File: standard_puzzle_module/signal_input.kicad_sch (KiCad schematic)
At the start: 6 parts, among them J9 Screw_Terminal_01x04

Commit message: chore: clean up
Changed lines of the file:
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@@
+	)
+	(junction
+		(at 134.62 107.95)
+		(diameter 0)
+		(color 0 0 0 0)
+	)
+	(junction
+		(at 134.62 96.52)
+		(diameter 0)
+		(color 0 0 0 0)
 	)
 	(junction
@@
 		(color 0 0 0 0)
 	)
-	(junction
-		(at 134.62 107.95)
-		(diameter 0)
-		(color 0 0 0 0)
-	)
-	(junction
-		(at 134.62 96.52)
-		(diameter 0)
-		(color 0 0 0 0)
-	)
 	(wire
 		(pts
@@
 	(wire
 		(pts
-			(xy 119.38 104.14) (xy 119.38 107.95)
+			(xy 102.87 107.95) (xy 119.38 107.95)
+		)
+		(stroke
+			(width 0)
+			(type default)
+		)
+	)
+	(wire
+		(pts
+			(xy 119.38 96.52) (xy 119.38 107.95)
 		)
 		(stroke
@@
 		(pts
 			(xy 147.32 107.95) (xy 162.56 107.95)
+		)
+		(stroke
+			(width 0)
+			(type default)
+		)
+	)
+	(wire
+		(pts
+			(xy 102.87 96.52) (xy 102.87 107.95)
 		)
 		(stroke
@@
 	(global_label "GPIO"
 		(shape input)
-		(at 119.38 104.14 90)
+		(at 119.38 96.52 90)
 		(fields_autoplaced yes)
 		(effects
@@
 		)
 		(property "Intersheetrefs" "${INTERSHEET_REFS}"
-			(at 119.38 96.6795 90)
+			(at 119.38 89.0595 90)
 			(hide yes)
 			(show_name no)
@@
 		)
 	)
+	(hierarchical_label "signal_input"
+		(shape output)
+		(at 102.87 96.52 0)
+		(effects
+			(font
+				(size 1.27 1.27)
+			)
+			(justify left)
+		)
+	)

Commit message: feat: clean up schematic references and run clean annotation
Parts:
- CC_SIN1: renamed from C13; footprint (none) -> Capacitor_THT:C_Disc_D5.0mm_W2.5mm_P5.00mm
- J_SIN1: renamed from J9; value Screw_Terminal_01x04 -> SIGNAL IN; footprint (none) -> TerminalBlock_Phoenix:TerminalBlock_Phoenix_MKDS-1,5-4-5.08_1x04_P5.08mm_Horizontal
- R_SIN1: renamed from R18; value 100 kOhm -> 100kOhm; footprint (none) -> Resistor_THT:R_Axial_DIN0411_L9.9mm_D3.6mm_P15.24mm_Horizontal
- R_SIN2: renamed from R19; value 4.7 kOhm -> 4.7kOhm; footprint (none) -> Resistor_THT:R_Axial_DIN0411_L9.9mm_D3.6mm_P15.24mm_Horizontal
- renumbered D9 to D_SCHSIN1, D10 to D_SCHSIN2
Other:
- moved on the sheet: CC_SIN1
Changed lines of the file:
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@@
 	(wire
 		(pts
-			(xy 119.38 120.65) (xy 119.38 118.11)
+			(xy 119.38 120.65) (xy 119.38 119.38)
 		)
 		(stroke
@@
 	(wire
 		(pts
-			(xy 119.38 110.49) (xy 119.38 107.95)
+			(xy 119.38 111.76) (xy 119.38 107.95)
 		)
 		(stroke
@@
 		(dnp no)
 		(fields_autoplaced yes)
-		(property "Reference" "J9"
+		(property "Reference" "J_SIN1"
 			(at 170.18 105.4099 0)
 			(show_name no)
@@
 			)
 		)
-		(property "Value" "Screw_Terminal_01x04"
+		(property "Value" "SIGNAL IN"
 			(at 170.18 107.9499 0)
 			(show_name no)
@@
 			)
 		)
-		(property "Footprint" ""
+		(property "Footprint" "TerminalBlock_Phoenix:TerminalBlock_Phoenix_MKDS-1,5-4-5.08_1x04_P5.08mm_Horizontal"
 			(at 167.64 105.41 0)
 			(hide yes)
@@
 		(instances
 			(project "standard_puzzle_box"
-				(path "/13314f97-080e-4924-a8fe-b4d224920625/c0b0d7d0-33da-4714-9ac3-d3e577314e9e"
-					(reference "J11")
+				(path "/13314f97-080e-4924-a8fe-b4d224920625/b204176e-3230-48f0-bf70-6ca27eccae57"
+					(reference "J_SIN2")
 					(unit 1)
 				)
 				(path "/13314f97-080e-4924-a8fe-b4d224920625/c2e63cb3-71db-41cb-b6d8-62c7e6a89138"
-					(reference "J9")
+					(reference "J_SIN1")
 					(unit 1)
 				)
@@
 		(dnp no)
 		(fields_autoplaced yes)
-		(property "Reference" "R19"
+		(property "Reference" "R_SIN2"
 			(at 143.51 101.6 90)
 			(show_name no)
@@
 			)
 		)
-		(property "Value" "4.7 kOhm"
+		(property "Value" "4.7kOhm"
 			(at 143.51 104.14 90)
 			(show_name no)
@@
 			)
 		)
-		(property "Footprint" ""
+		(property "Footprint" "Resistor_THT:R_Axial_DIN0411_L9.9mm_D3.6mm_P15.24mm_Horizontal"
 			(at 143.51 106.172 90)
 			(hide yes)
@@
 		(instances
 			(project "standard_puzzle_box"
-				(path "/13314f97-080e-4924-a8fe-b4d224920625/c0b0d7d0-33da-4714-9ac3-d3e577314e9e"
-					(reference "R21")
+				(path "/13314f97-080e-4924-a8fe-b4d224920625/b204176e-3230-48f0-bf70-6ca27eccae57"
+					(reference "R_SIN4")
 					(unit 1)
 				)
 				(path "/13314f97-080e-4924-a8fe-b4d224920625/c2e63cb3-71db-41cb-b6d8-62c7e6a89138"
-					(reference "R19")
+					(reference "R_SIN2")
 					(unit 1)
 				)
@@
 		(instances
 			(project "standard_puzzle_box"
-				(path "/13314f97-080e-4924-a8fe-b4d224920625/c0b0d7d0-33da-4714-9ac3-d3e577314e9e"
-					(reference "#PWR051")
+				(path "/13314f97-080e-4924-a8fe-b4d224920625/b204176e-3230-48f0-bf70-6ca27eccae57"
+					(reference "#PWR01")
 					(unit 1)
 				)
@@
 		)
 		(property "Value" "+3.3V"
-			(at 144.526 90.17 0)
+			(at 148.59 95.25 0)
 			(show_name no)
 			(do_not_autoplace no)
@@
 		(instances
 			(project "standard_puzzle_box"
-				(path "/13314f97-080e-4924-a8fe-b4d224920625/c0b0d7d0-33da-4714-9ac3-d3e577314e9e"
-					(reference "#PWR054")
+				(path "/13314f97-080e-4924-a8fe-b4d224920625/b204176e-3230-48f0-bf70-6ca27eccae57"
+					(reference "#PWR011")
 					(unit 1)
 				)
@@
 		(instances
 			(project "standard_puzzle_box"
-				(path "/13314f97-080e-4924-a8fe-b4d224920625/c0b0d7d0-33da-4714-9ac3-d3e577314e9e"
-					(reference "#PWR052")
+				(path "/13314f97-080e-4924-a8fe-b4d224920625/b204176e-3230-48f0-bf70-6ca27eccae57"
+					(reference "#PWR09")
 					(unit 1)
 				)
@@
 		(in_pos_files yes)
 		(dnp no)
-		(fields_autoplaced yes)
-		(property "Reference" "D10"
-			(at 140.0175 90.17 0)
+		(property "Reference" "D_SCHSIN2"
+			(at 140.97 90.17 0)
 			(show_name no)
 			(do_not_autoplace no)
@@
 		(instances
 			(project "standard_puzzle_box"
-				(path "/13314f97-080e-4924-a8fe-b4d224920625/c0b0d7d0-33da-4714-9ac3-d3e577314e9e"
-					(reference "D14")
+				(path "/13314f97-080e-4924-a8fe-b4d224920625/b204176e-3230-48f0-bf70-6ca27eccae57"
+					(reference "D_SCHSIN4")
 					(unit 1)
 				)
 				(path "/13314f97-080e-4924-a8fe-b4d224920625/c2e63cb3-71db-41cb-b6d8-62c7e6a89138"
-					(reference "D10")
+					(reference "D_SCHSIN2")
 					(unit 1)
 				)
@@
 		(in_pos_files yes)
 		(dnp no)
-		(fields_autoplaced yes)
-		(property "Reference" "D9"
-			(at 129.8575 90.17 0)
+		(property "Reference" "D_SCHSIN1"
+			(at 128.27 90.17 0)
 			(show_name no)
 			(do_not_autoplace no)
@@
 		(instances
 			(project "standard_puzzle_box"
-				(path "/13314f97-080e-4924-a8fe-b4d224920625/c0b0d7d0-33da-4714-9ac3-d3e577314e9e"
-					(reference "D13")
+				(path "/13314f97-080e-4924-a8fe-b4d224920625/b204176e-3230-48f0-bf70-6ca27eccae57"
+					(reference "D_SCHSIN3")
 					(unit 1)
 				)
 				(path "/13314f97-080e-4924-a8fe-b4d224920625/c2e63cb3-71db-41cb-b6d8-62c7e6a89138"
-					(reference "D9")
+					(reference "D_SCHSIN1")
 					(unit 1)
 				)
@@
 		(instances
 			(project "standard_puzzle_box"
-				(path "/13314f97-080e-4924-a8fe-b4d224920625/c0b0d7d0-33da-4714-9ac3-d3e577314e9e"
-					(reference "#PWR055")
+				(path "/13314f97-080e-4924-a8fe-b4d224920625/b204176e-3230-48f0-bf70-6ca27eccae57"
+					(reference "#PWR012")
 					(unit 1)
 				)
@@
 		(dnp no)
 		(fields_autoplaced yes)
-		(property "Reference" "R18"
+		(property "Reference" "R_SIN1"
 			(at 137.16 114.2999 0)
 			(show_name no)
@@
 			)
 		)
-		(property "Value" "100 kOhm"
+		(property "Value" "100kOhm"
 			(at 137.16 116.8399 0)
 			(show_name no)
@@
 			)
 		)
-		(property "Footprint" ""
+		(property "Footprint" "Resistor_THT:R_Axial_DIN0411_L9.9mm_D3.6mm_P15.24mm_Horizontal"
 			(at 132.842 115.57 90)
 			(hide yes)
@@
 		(instances
 			(project "standard_puzzle_box"
-				(path "/13314f97-080e-4924-a8fe-b4d224920625/c0b0d7d0-33da-4714-9ac3-d3e577314e9e"
-					(reference "R20")
+				(path "/13314f97-080e-4924-a8fe-b4d224920625/b204176e-3230-48f0-bf70-6ca27eccae57"
+					(reference "R_SIN3")
 					(unit 1)
 				)
 				(path "/13314f97-080e-4924-a8fe-b4d224920625/c2e63cb3-71db-41cb-b6d8-62c7e6a89138"
-					(reference "R18")
+					(reference "R_SIN1")
 					(unit 1)
 				)
@@
 	(symbol
 		(lib_id "Device:C")
-		(at 119.38 114.3 0)
+		(at 119.38 115.57 0)
 		(unit 1)
 		(body_style 1)
@@
 		(in_pos_files yes)
 		(dnp no)
-		(property "Reference" "C13"
-			(at 123.698 113.792 0)
+		(property "Reference" "CC_SIN1"
+			(at 125.73 114.3 0)
 			(show_name no)
 			(do_not_autoplace no)
@@
 		)
 		(property "Value" "10nF"
-			(at 125.222 116.078 0)
-			(show_name no)
-			(do_not_autoplace no)
-			(effects
-				(font
-					(size 1.27 1.27)
-				)
-			)
-		)
-		(property "Footprint" ""
-			(at 120.3452 118.11 0)
+			(at 125.73 116.84 0)
+			(show_name no)
+			(do_not_autoplace no)
+			(effects
+				(font
+					(size 1.27 1.27)
+				)
+			)
+		)
+		(property "Footprint" "Capacitor_THT:C_Disc_D5.0mm_W2.5mm_P5.00mm"
+			(at 120.3452 119.38 0)
 			(hide yes)
 			(show_name no)
@@
 		)
 		(property "Datasheet" ""
-			(at 119.38 114.3 0)
+			(at 119.38 115.57 0)
 			(hide yes)
 			(show_name no)
@@
 		)
 		(property "Description" "Unpolarized capacitor"
-			(at 119.38 114.3 0)
+			(at 119.38 115.57 0)
 			(hide yes)
 			(show_name no)
@@
 		(instances
 			(project "standard_puzzle_box"
-				(path "/13314f97-080e-4924-a8fe-b4d224920625/c0b0d7d0-33da-4714-9ac3-d3e577314e9e"
-					(reference "C17")
+				(path "/13314f97-080e-4924-a8fe-b4d224920625/b204176e-3230-48f0-bf70-6ca27eccae57"
+					(reference "CC_SIN2")
 					(unit 1)
 				)
 				(path "/13314f97-080e-4924-a8fe-b4d224920625/c2e63cb3-71db-41cb-b6d8-62c7e6a89138"
-					(reference "C13")
+					(reference "CC_SIN1")
 					(unit 1)
 				)
@@
 		(instances
 			(project "standard_puzzle_box"
-				(path "/13314f97-080e-4924-a8fe-b4d224920625/c0b0d7d0-33da-4714-9ac3-d3e577314e9e"
-					(reference "#PWR057")
+				(path "/13314f97-080e-4924-a8fe-b4d224920625/b204176e-3230-48f0-bf70-6ca27eccae57"
+					(reference "#PWR014")
 					(unit 1)
 				)
@@
 		(instances
 			(project "standard_puzzle_box"
-				(path "/13314f97-080e-4924-a8fe-b4d224920625/c0b0d7d0-33da-4714-9ac3-d3e577314e9e"
-					(reference "#PWR053")
+				(path "/13314f97-080e-4924-a8fe-b4d224920625/b204176e-3230-48f0-bf70-6ca27eccae57"
+					(reference "#PWR010")
 					(unit 1)
 				)
@@
 		(instances
 			(project "standard_puzzle_box"
-				(path "/13314f97-080e-4924-a8fe-b4d224920625/c0b0d7d0-33da-4714-9ac3-d3e577314e9e"
-					(reference "#PWR056")
-					(unit 1)
-				)
+				(path "/13314f97-080e-4924-a8fe-b4d224920625/b204176e-3230-48f0-bf70-6ca27eccae57"
+					(reference "#PWR013")
+					(unit 1)
+				)

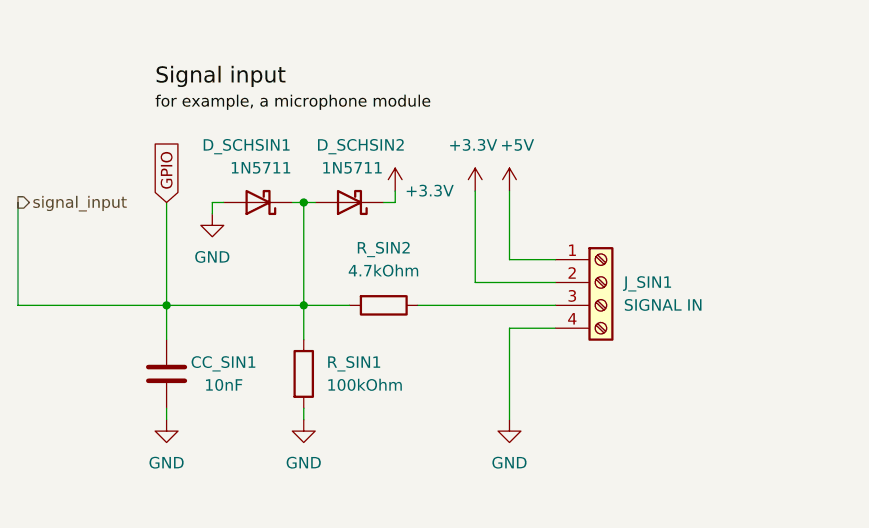
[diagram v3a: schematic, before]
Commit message: fix: run erc and fix errors and warnings
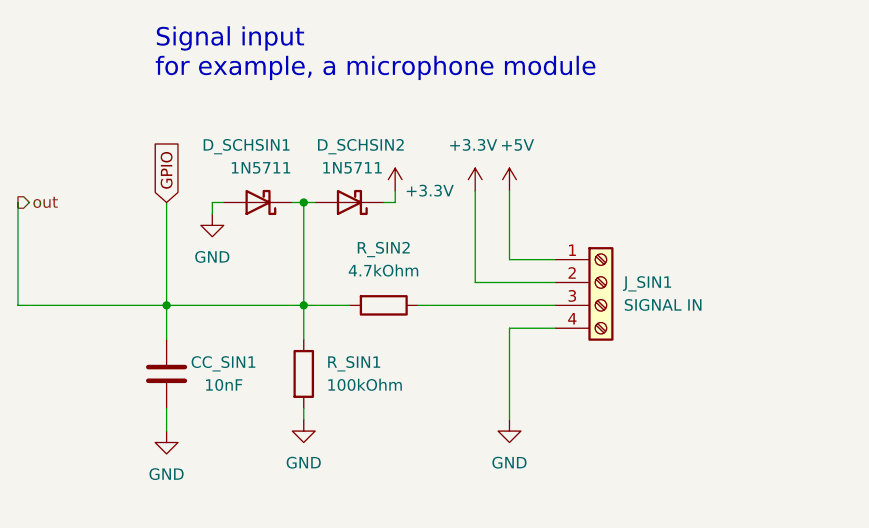
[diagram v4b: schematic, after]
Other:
- note added: "Signal input for example, a microphone module"
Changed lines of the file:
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@@
 		(title "Signal input")
+	)
+	(text "Signal input\nfor example, a microphone module\n"
+		(exclude_from_sim no)
+		(at 118.11 80.01 0)
+		(effects
+			(font
+				(size 2.032 2.032)
+				(color 255 97 9 1)
+			)
+			(justify left)
+		)
 	)
 	(junction
@@
 	(wire
 		(pts
-			(xy 119.38 120.65) (xy 119.38 119.38)
-		)
-		(stroke
-			(width 0)
-			(type default)
-		)
-	)
-	(wire
-		(pts
 			(xy 157.48 95.25) (xy 157.48 102.87)
 		)
@@
 	(wire
 		(pts
+			(xy 119.38 119.38) (xy 119.38 121.92)
+		)
+		(stroke
+			(width 0)
+			(type default)
+		)
+	)
+	(wire
+		(pts
 			(xy 157.48 110.49) (xy 157.48 120.65)
 		)
@@
 			(width 0)
 			(type default)
-		)
-	)
-	(label "for example, a microphone module"
-		(at 118.11 86.36 0)
-		(effects
-			(font
-				(size 1.27 1.27)
-			)
-			(justify left bottom)
-		)
-	)
-	(label "Signal input"
-		(at 118.11 83.82 0)
-		(effects
-			(font
-				(size 1.778 1.778)
-			)
-			(justify left bottom)
 		)
 	)
@@
 		)
 	)
-	(hierarchical_label "signal_input"
+	(hierarchical_label "out"
 		(shape output)
 		(at 102.87 96.52 0)
@@
 	(symbol
 		(lib_id "power:GND")
-		(at 119.38 120.65 0)
+		(at 119.38 121.92 0)
 		(unit 1)
 		(body_style 1)
@@
 		(dnp no)
 		(property "Reference" "#PWR042"
-			(at 119.38 127 0)
+			(at 119.38 128.27 0)
 			(hide yes)
 			(show_name no)
@@
 		)
 		(property "Value" "GND"
-			(at 119.38 125.476 0)
+			(at 119.38 126.746 0)
 			(show_name no)
 			(do_not_autoplace no)
@@
 		)
 		(property "Footprint" ""
-			(at 119.38 120.65 0)
+			(at 119.38 121.92 0)
 			(hide yes)
 			(show_name no)
@@
 		)
 		(property "Datasheet" ""
-			(at 119.38 120.65 0)
+			(at 119.38 121.92 0)
 			(hide yes)
 			(show_name no)
@@
 		)
 		(property "Description" "Power symbol creates a global label with name \"GND\" , ground"
-			(at 119.38 120.65 0)
-			(hide yes)
-			(show_name no)
+			(at 119.38 121.92 0)
+			(hide yes)
+			(show_name no)

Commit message: feat: dump working files before blackout
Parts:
- R_SIN1: value 100kOhm -> 100k
- R_SIN2: value 4.7kOhm -> 4.7k
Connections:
- net GPIO renamed out
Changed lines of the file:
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@@
 	(wire
 		(pts
-			(xy 119.38 96.52) (xy 119.38 107.95)
+			(xy 119.38 119.38) (xy 119.38 124.46)
 		)
 		(stroke
@@
 	(wire
 		(pts
-			(xy 119.38 119.38) (xy 119.38 121.92)
-		)
-		(stroke
-			(width 0)
-			(type default)
-		)
-	)
-	(wire
-		(pts
 			(xy 157.48 110.49) (xy 157.48 120.65)
 		)
@@
 			(width 0)
 			(type default)
-		)
-	)
-	(global_label "GPIO"
-		(shape input)
-		(at 119.38 96.52 90)
-		(fields_autoplaced yes)
-		(effects
-			(font
-				(size 1.27 1.27)
-			)
-			(justify left)
-		)
-		(property "Intersheetrefs" "${INTERSHEET_REFS}"
-			(at 119.38 89.0595 90)
-			(hide yes)
-			(show_name no)
-			(do_not_autoplace no)
-			(effects
-				(font
-					(size 1.27 1.27)
-				)
-				(justify left)
-			)
 		)
 	)
@@
 			)
 		)
-		(property "Value" "4.7kOhm"
+		(property "Value" "4.7k"
 			(at 143.51 104.14 90)
 			(show_name no)
@@
 	(symbol
 		(lib_id "power:GND")
-		(at 119.38 121.92 0)
+		(at 119.38 124.46 0)
 		(unit 1)
 		(body_style 1)
@@
 		(dnp no)
 		(property "Reference" "#PWR042"
-			(at 119.38 128.27 0)
+			(at 119.38 130.81 0)
 			(hide yes)
 			(show_name no)
@@
 		)
 		(property "Value" "GND"
-			(at 119.38 126.746 0)
+			(at 119.38 129.286 0)
 			(show_name no)
 			(do_not_autoplace no)
@@
 		)
 		(property "Footprint" ""
-			(at 119.38 121.92 0)
+			(at 119.38 124.46 0)
 			(hide yes)
 			(show_name no)
@@
 		)
 		(property "Datasheet" ""
-			(at 119.38 121.92 0)
+			(at 119.38 124.46 0)
 			(hide yes)
 			(show_name no)
@@
 		)
 		(property "Description" "Power symbol creates a global label with name \"GND\" , ground"
-			(at 119.38 121.92 0)
+			(at 119.38 124.46 0)
 			(hide yes)
 			(show_name no)
@@
 			)
 		)
-		(property "Value" "100kOhm"
+		(property "Value" "100k"
 			(at 137.16 116.8399 0)
 			(show_name no)
